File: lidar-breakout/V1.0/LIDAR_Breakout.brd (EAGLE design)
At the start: 36.5 x 88 mm, 96 parts, among them P1 MOLEX 0436500200, X1 TSX-3225 16.0000MF18X-AC0

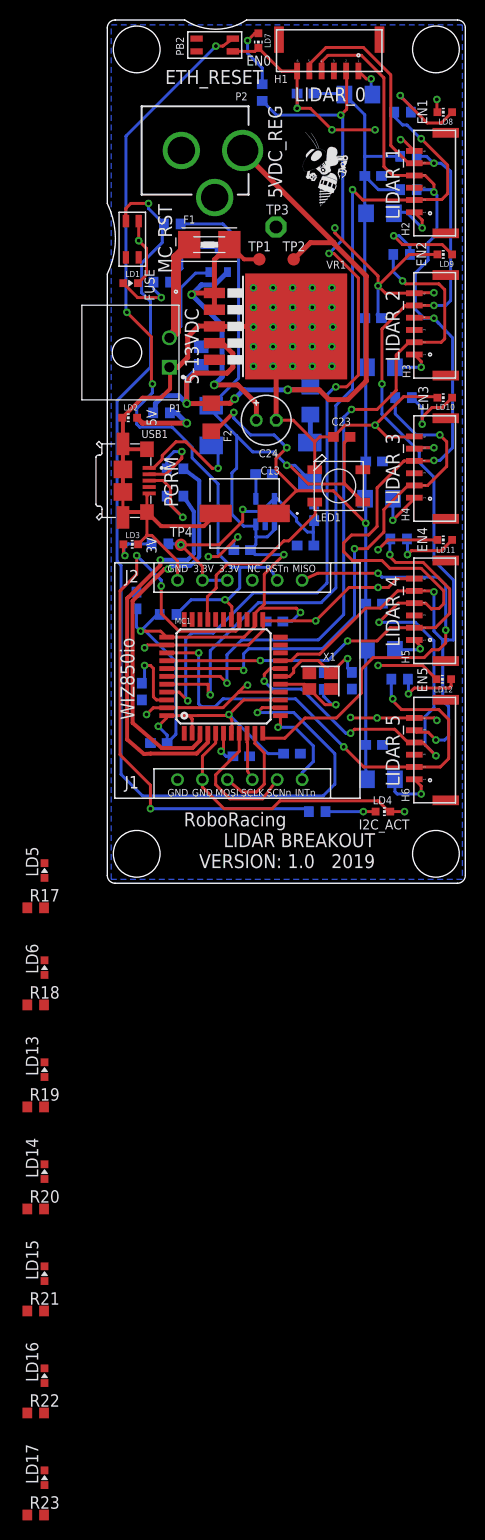
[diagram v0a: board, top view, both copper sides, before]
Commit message: Branch Cleanup, Rev 1.1 Updates
Added I2C IO expander and resistor array for new leds.
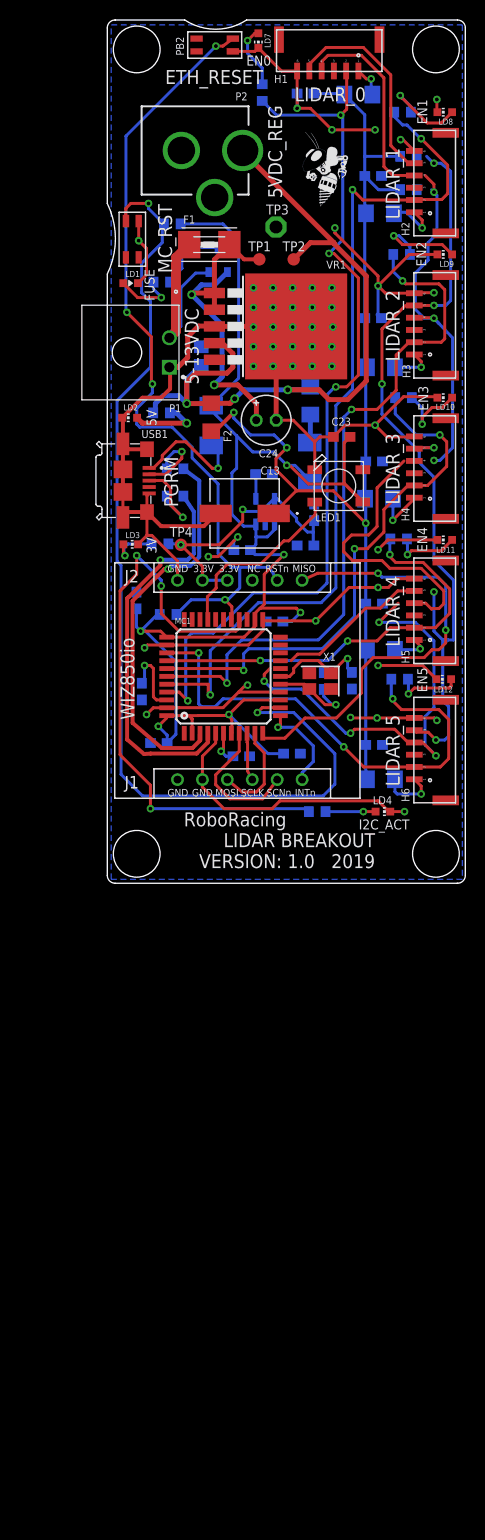
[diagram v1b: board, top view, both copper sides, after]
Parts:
- removed LD13, LD14, LD15, LD16, LD17, LD5, LD6: RED, RoboJackets-LEDs:CHIP-LED0603
- removed R17, R18, R19, R20, R21, R22, R23: 1 kΩ, rcl:R0603
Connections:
- net SCL_LIDAR renamed SCL
- net SDA_LIDAR renamed SDA
- removed net COMM_ERR: R17.1
- removed net LDR2_ERR: R19.1
- removed net LDR6_ERR: R18.1, R20.1, R21.1, R22.1, R23.1
- removed net N$10: LD6.A, R18.2
- removed net N$11: LD13.A, R19.2
- removed net N$12: LD14.A, R20.2
- removed net N$13: LD15.A, R21.2
- removed net N$14: LD16.A, R22.2
- removed net N$15: LD17.A, R23.2
- removed net N$9: LD5.A, R17.2
- net GND: no longer LD13.C, LD14.C, LD15.C, LD16.C, LD17.C, LD5.C, LD6.C
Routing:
- net SCL: track 139.9 -> 131.5 mm
- net SDA: track 127.2 -> 119.5 mm
